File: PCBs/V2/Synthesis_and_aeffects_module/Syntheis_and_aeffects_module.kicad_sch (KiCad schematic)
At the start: 34 parts, among them J1(AudioJack)1 Conn_01x03, J2(IN)1 IN, J3(OUT)1 OUT, U1 STM32H750VBTx, U2 TPA6110A2DGN

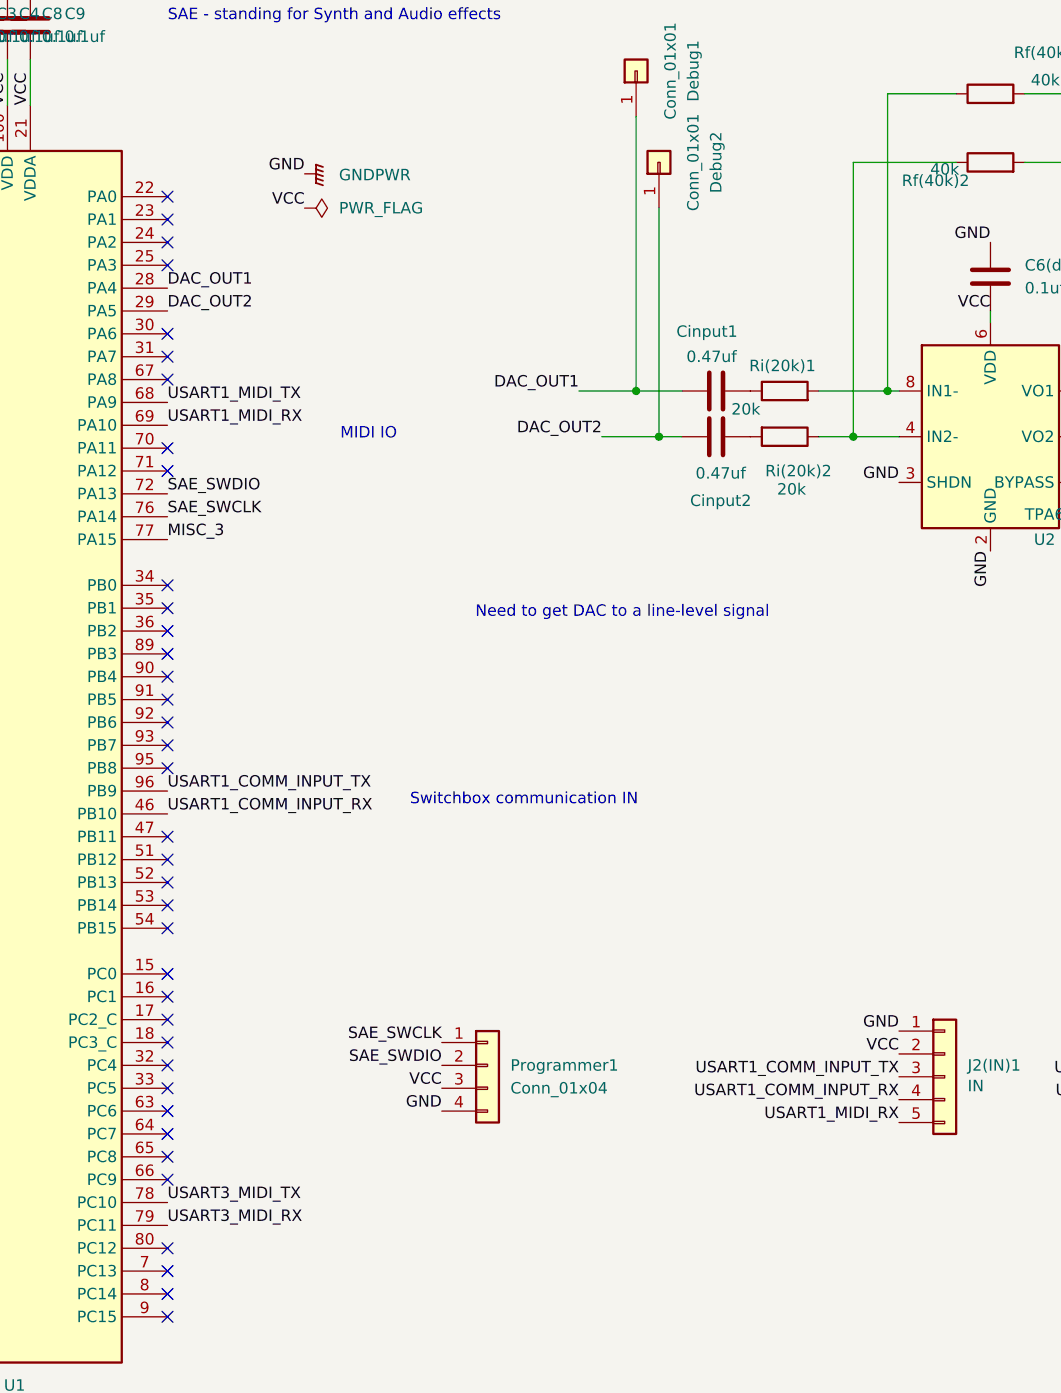
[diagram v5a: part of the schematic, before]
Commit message: messed UART connection for synthesis PCB :/ good thing i had those misc pads for testing. Need to reorder.
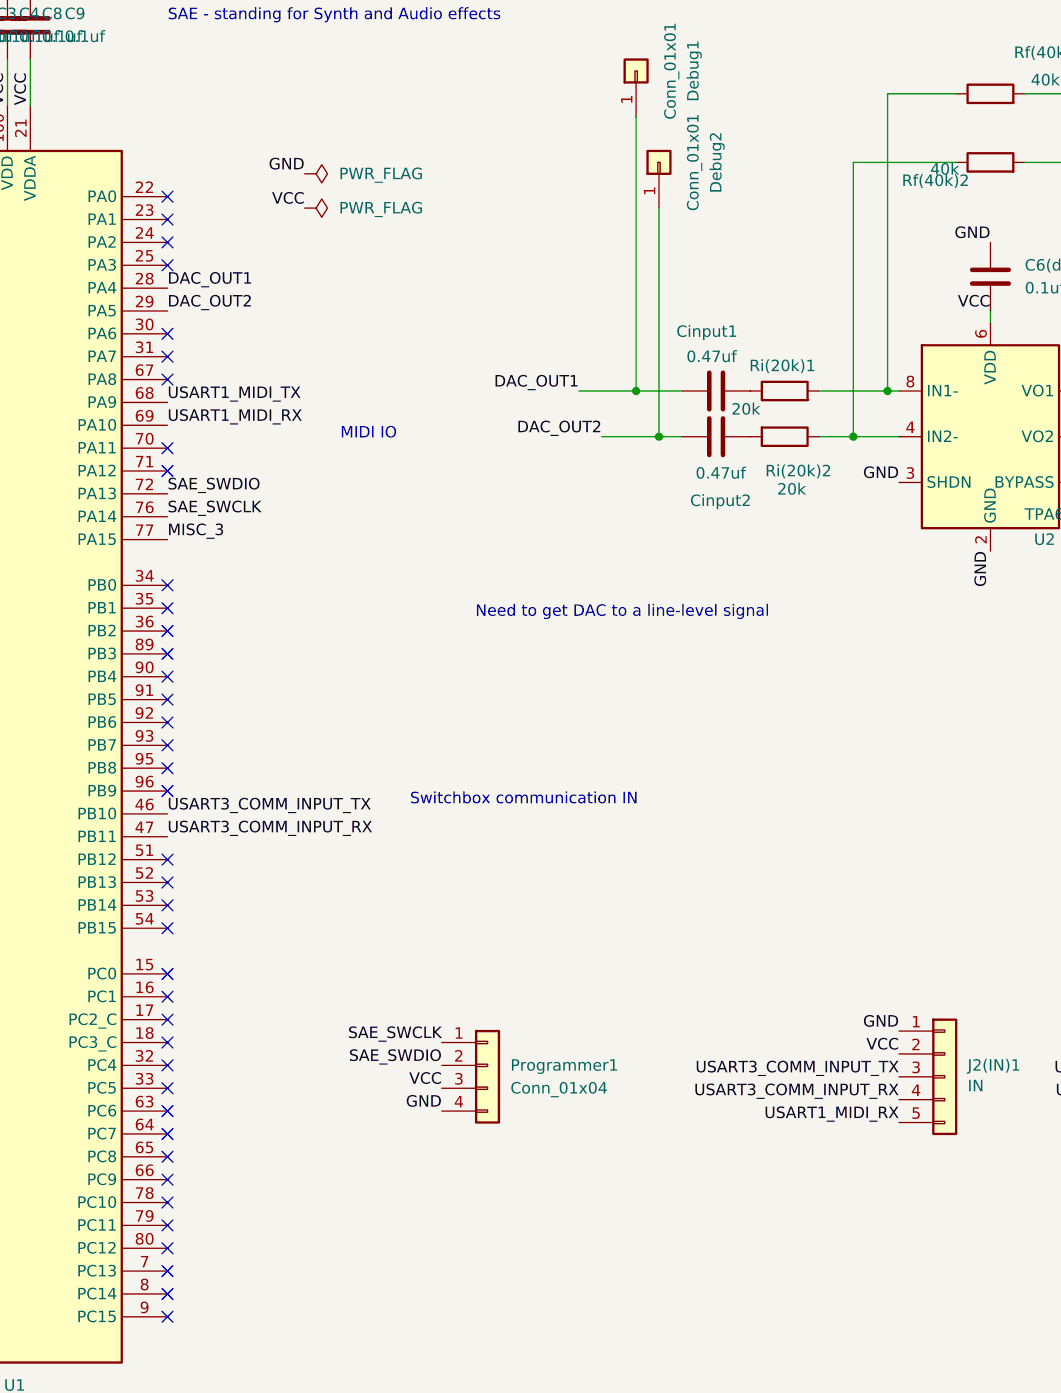
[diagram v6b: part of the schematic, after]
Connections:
- net USART3_COMM_INPUT_RX: now reaches U1.47 (PB11)
- net USART3_COMM_INPUT_RX: now also J2(IN)1.4 (Pin_4)
- net GNDPWR renamed GND
- net USART1_COMM_INPUT_RX renamed USART3_COMM_INPUT_TX
- net USART3_COMM_INPUT_TX: now also J2(IN)1.3 (Pin_3); no longer J2(IN)1.4 (Pin_4)
- net USART1_COMM_INPUT_TX: no longer names the net of U1.96 (PB9)
- net USART1_COMM_INPUT_TX: no longer J2(IN)1.3 (Pin_3)
- net USART3_MIDI_RX: no longer names the net of U1.79 (PC11)
- net USART3_MIDI_TX: no longer names the net of U1.78 (PC10)
- no-connect marks 68 -> 70
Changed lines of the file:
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@@
-	)
-	(no_connect
-		(at 125.73 118.11)
 	)
 	(no_connect
@@
 	)
 	(no_connect
+		(at 125.73 113.03)
+	)
+	(no_connect
 		(at 125.73 100.33)
 	)
@@
 	)
 	(no_connect
+		(at 125.73 158.75)
+	)
+	(no_connect
 		(at 80.01 69.85)
 	)
@@
 	(no_connect
 		(at 80.01 151.13)
+	)
+	(no_connect
+		(at 125.73 161.29)
 	)
 	(no_connect
@@
 		)
 	)
-	(label "USART1_COMM_INPUT_RX"
-		(at 125.73 115.57 0)
-		(effects
-			(font
-				(size 1.27 1.27)
-			)
-			(justify left bottom)
-		)
-	)
-	(label "USART1_COMM_INPUT_TX"
-		(at 125.73 113.03 0)
-		(effects
-			(font
-				(size 1.27 1.27)
-			)
-			(justify left bottom)
-		)
-	)
 	(label "VCC"
 		(at 207.01 142.24 180)
@@
 		)
 	)
-	(label "USART1_COMM_INPUT_RX"
+	(label "USART3_COMM_INPUT_RX"
 		(at 207.01 147.32 180)
 		(effects
@@
 		)
 	)
-	(label "USART3_MIDI_RX"
-		(at 125.73 161.29 0)
-		(effects
-			(font
-				(size 1.27 1.27)
-			)
-			(justify left bottom)
-		)
-	)
 	(label "DAC_OUT1"
 		(at 125.73 57.15 0)
@@
 		)
 	)
+	(label "USART3_COMM_INPUT_RX"
+		(at 125.73 118.11 0)
+		(effects
+			(font
+				(size 1.27 1.27)
+			)
+			(justify left bottom)
+		)
+	)
 	(label "AudioJack_T"
 		(at 262.89 69.85 0)
@@
 		)
 	)
+	(label "USART3_COMM_INPUT_TX"
+		(at 125.73 115.57 0)
+		(effects
+			(font
+				(size 1.27 1.27)
+			)
+			(justify left bottom)
+		)
+	)
 	(label "VCC"
 		(at 97.79 36.83 90)
@@
 		)
 	)
-	(label "USART1_COMM_INPUT_TX"
+	(label "USART3_COMM_INPUT_TX"
 		(at 207.01 144.78 180)
 		(effects
@@
 			)
 			(justify right bottom)
-		)
-	)
-	(label "USART3_MIDI_TX"
-		(at 125.73 158.75 0)
-		(effects
-			(font
-				(size 1.27 1.27)
-			)
-			(justify left bottom)
 		)
 	)
@@
 	)
 	(symbol
-		(lib_id "power:GNDPWR")
-		(at 140.97 44.45 90)
-		(unit 1)
-		(exclude_from_sim no)
-		(in_bom yes)
-		(on_board yes)
-		(dnp no)
-		(fields_autoplaced yes)
-		(property "Reference" "#PWR01"
-			(at 146.05 44.45 0)
-			(effects
-				(font
-					(size 1.27 1.27)
-				)
-				(hide yes)
-			)
-		)
-		(property "Value" "GNDPWR"
-			(at 144.78 44.5769 90)
-			(effects
-				(font
-					(size 1.27 1.27)
-				)
-				(justify right)
-			)
-		)
-		(property "Footprint" ""
-			(at 142.24 44.45 0)
-			(effects
-				(font
-					(size 1.27 1.27)
-				)
-				(hide yes)
-			)
-		)
-		(property "Datasheet" ""
-			(at 142.24 44.45 0)
-			(effects
-				(font
-					(size 1.27 1.27)
-				)
-				(hide yes)
-			)
-		)
-		(property "Description" "Power symbol creates a global label with name \"GNDPWR\" , global ground"
-			(at 140.97 44.45 0)
-			(effects
-				(font
-					(size 1.27 1.27)
-				)
-				(hide yes)
-			)
-		)
-		(pin "1"
-		)
-		(instances
-			(project ""
-				(path "/edf9ac54-8c23-46ef-867e-bfab8959c07a"
-					(reference "#PWR01")
-					(unit 1)
-				)
-			)
-		)
-	)
-	(symbol
 		(lib_id "Device:C")
 		(at 228.6 100.33 0)
@@
 					(unit 1)
 				)
+			)
+		)
+	)
+	(symbol
+		(lib_id "power:PWR_FLAG")
+		(at 140.97 44.45 270)
+		(unit 1)
+		(exclude_from_sim no)
+		(in_bom yes)
+		(on_board yes)
+		(dnp no)
+		(fields_autoplaced yes)
+		(property "Reference" "#FLG02"
+			(at 142.875 44.45 0)
+			(effects
+				(font
+					(size 1.27 1.27)
+				)
+				(hide yes)
+			)
+		)
+		(property "Value" "PWR_FLAG"
+			(at 144.78 44.4499 90)
+			(effects
+				(font
+					(size 1.27 1.27)
+				)
+				(justify left)
+			)
+		)
+		(property "Footprint" ""
+			(at 140.97 44.45 0)
+			(effects
+				(font
+					(size 1.27 1.27)
+				)
+				(hide yes)
+			)
+		)
+		(property "Datasheet" "~"
+			(at 140.97 44.45 0)
+			(effects
+				(font
+					(size 1.27 1.27)
+				)
+				(hide yes)
+			)
+		)
+		(property "Description" "Special symbol for telling ERC where power comes from"
+			(at 140.97 44.45 0)
+			(effects
+				(font
+					(size 1.27 1.27)
+				)
+				(hide yes)
+			)
+		)
+		(pin "1"
+		)
+		(instances
+			(project "Syntheis_and_aeffects_module"
+				(path "/edf9ac54-8c23-46ef-867e-bfab8959c07a"
+					(reference "#FLG02")
+					(unit 1)
+				)
